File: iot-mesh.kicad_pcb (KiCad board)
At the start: 2 copper layers, 73 x 39 mm, 18 parts, among them J1 DS18B20 connector, J2 BME280 connector, J5 Power Connector, U1 XIAO-nRF52840-DIP, U2 WEMOS_D1_mini, U3 L7805

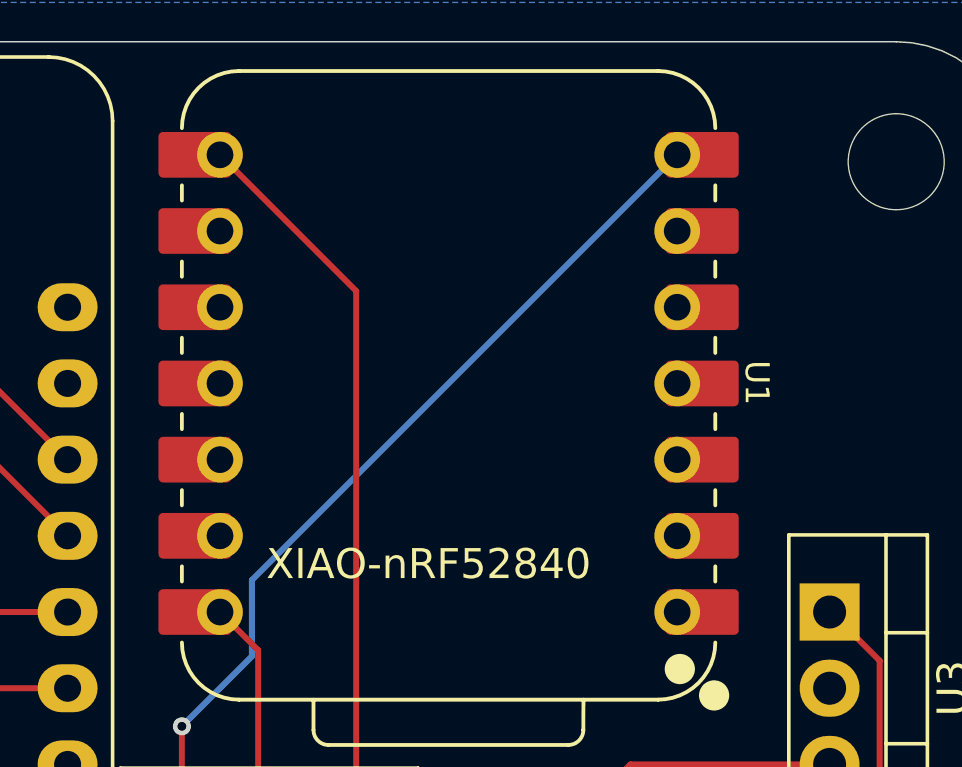
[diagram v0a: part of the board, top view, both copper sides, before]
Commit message: Add project specific symbol and footprint
XIAO-nRF52840-DIP is modified so that silkscreen does not go over pads.
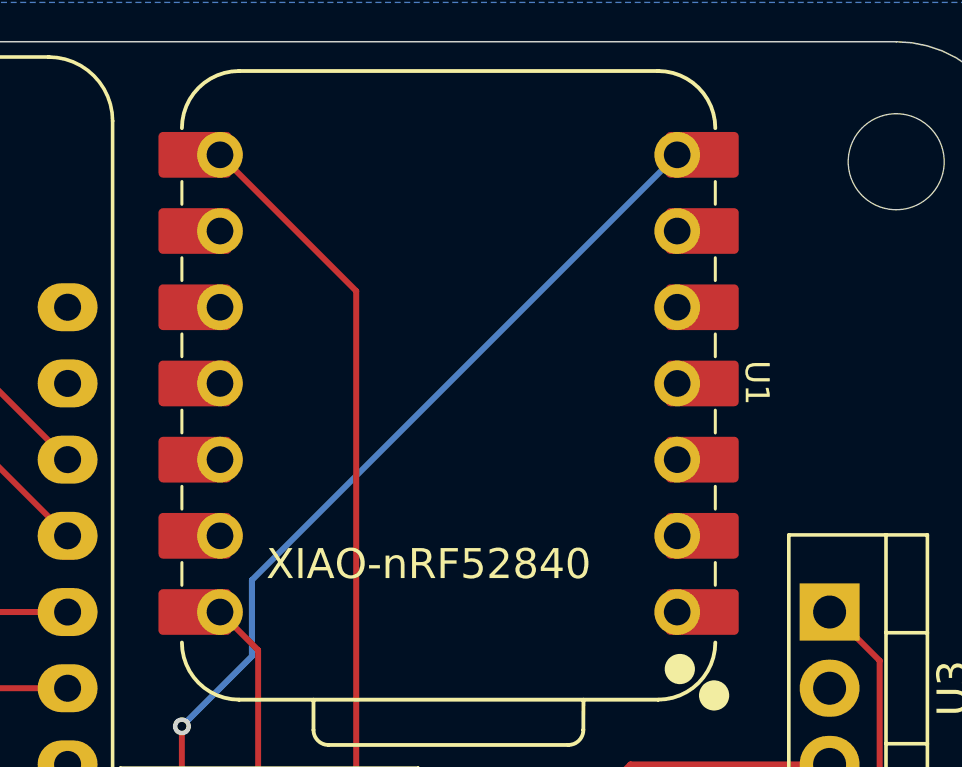
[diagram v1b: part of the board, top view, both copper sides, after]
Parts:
- U1: footprint XIAO_Series_Footprints:XIAO-nRF52840-DIP-mod -> footprints:XIAO-nRF52840-DIP-mk
